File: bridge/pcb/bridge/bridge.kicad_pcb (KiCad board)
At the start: 2 copper layers, 108 x 80 mm, 26 parts, among them J1 Screw_Terminal_01x06, J2 Screw_Terminal_01x06, J3 Screw_Terminal_01x06, J4 Conn_01x23, J5 Conn_01x04, J6 Conn_01x02, J7 Conn_01x03, J8 Conn_01x02, J9 MCU_Test_Point, SW1 SW_SPST, U1 L293, U2 J104D2C12VDC.20S, U3 AD557JN, U4 ATmega328P-P

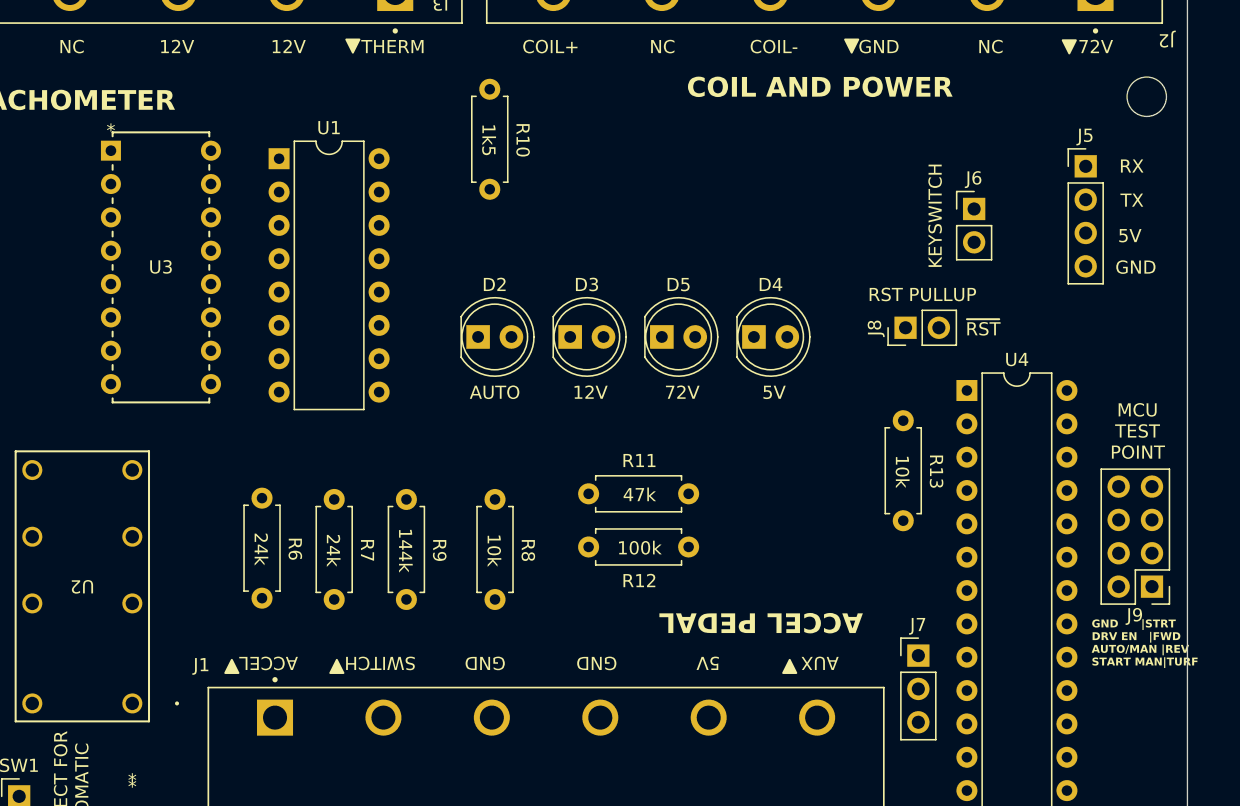
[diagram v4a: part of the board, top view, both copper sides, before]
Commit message: Assigned footprints and layed out board
Removed 5V and 12V enable headers as they added unneeded complexity
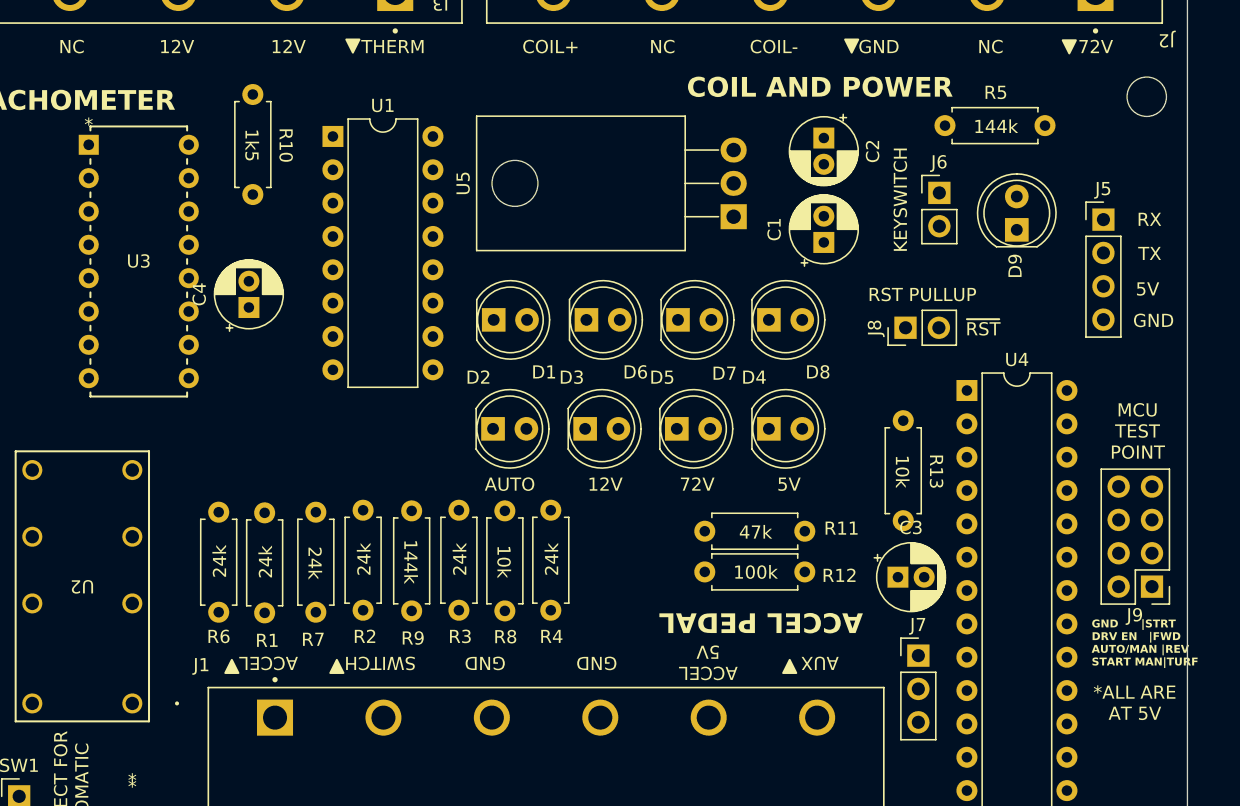
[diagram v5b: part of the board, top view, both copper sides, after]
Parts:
- added C1: 1u, Capacitor_THT:CP_Radial_D5.0mm_P2.00mm, F.Cu at (143.3, 72.8)
- added C2: 1u, Capacitor_THT:CP_Radial_D5.0mm_P2.00mm, F.Cu at (143.3, 64.8)
- added C3: 1u, Capacitor_THT:CP_Radial_D5.0mm_P2.00mm, F.Cu at (148.9, 98.3)
- added C4: 1u, Capacitor_THT:CP_Radial_D5.0mm_P2.00mm, F.Cu at (99.5, 77.8)
- added D1: GREEN, LED_THT:LED_D5.0mm, F.Cu at (118.2, 78.7)
- added D6: GREEN, LED_THT:LED_D5.0mm, F.Cu at (125.2, 78.7)
- added D7: GREEN, LED_THT:LED_D5.0mm, F.Cu at (132.2, 78.7)
- added D8: GREEN, LED_THT:LED_D5.0mm, F.Cu at (139.1, 78.7)
- added D9: GREEN, LED_THT:LED_D5.0mm, F.Cu at (158.0, 71.8)
- added R1: 24k, bridge:THT_RESISTOR_WITH_VALUE, F.Cu at (100.8, 97.2)
- added R2: 24k, bridge:THT_RESISTOR_WITH_VALUE, F.Cu at (108.3, 97.0)
- added R3: 24k, bridge:THT_RESISTOR_WITH_VALUE, F.Cu at (115.6, 97.0)
- added R4: 24k, bridge:THT_RESISTOR_WITH_VALUE, F.Cu at (122.6, 97.0)
- added R5: 144k, bridge:THT_RESISTOR_WITH_VALUE, F.Cu at (156.4, 64.0)
- added U5: L7805, Package_TO_SOT_THT:TO-220-3_Horizontal_TabDown, F.Cu at (136.4, 70.8)
- D2: value GREEN -> YELLOW
- D3, D4, D5: value GREEN -> RED
- moved R10 18.1 mm to (99.7, 65.4)
- moved R11 9.30 mm to (138.1, 94.9)
- moved R12 9.05 mm to (138.1, 98.0)
- moved D4 7.09 mm to (139.1, 87.0)
- moved D2 7.09 mm to (118.1, 87.0)
- moved D3 7.09 mm to (125.1, 87.0)
- moved D5 7.09 mm to (132.1, 87.0)
- moved U1 4.44 mm to (105.9, 64.7)
- moved J5 4.28 mm to (164.6, 71.1)
- moved R6 3.24 mm to (97.3, 97.1), turned to 90 degrees
- moved J6 2.92 mm to (152.1, 69.0)
- moved U3 1.75 mm to (87.3, 65.4)
- moved R7 1.70 mm to (104.5, 97.2)
- moved R8 1.15 mm to (118.9, 97.1)
- moved R9 0.96 mm to (111.8, 97.1)
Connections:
- J1 pad 5: +5V -> ACCEL_POT_5V
- J4 pad 9: +5V -> ACCEL_POT_5V
- U4 pad 25: unconnected-(U4-PC2-Pad25) -> ACCEL_POT_AUX
- U4 pad 26: unconnected-(U4-PC3-Pad26) -> ACCEL_AUX_MAN
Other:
- board text added: "*ALL ARE AT 5V"
- board text added: "ACCEL 5V"

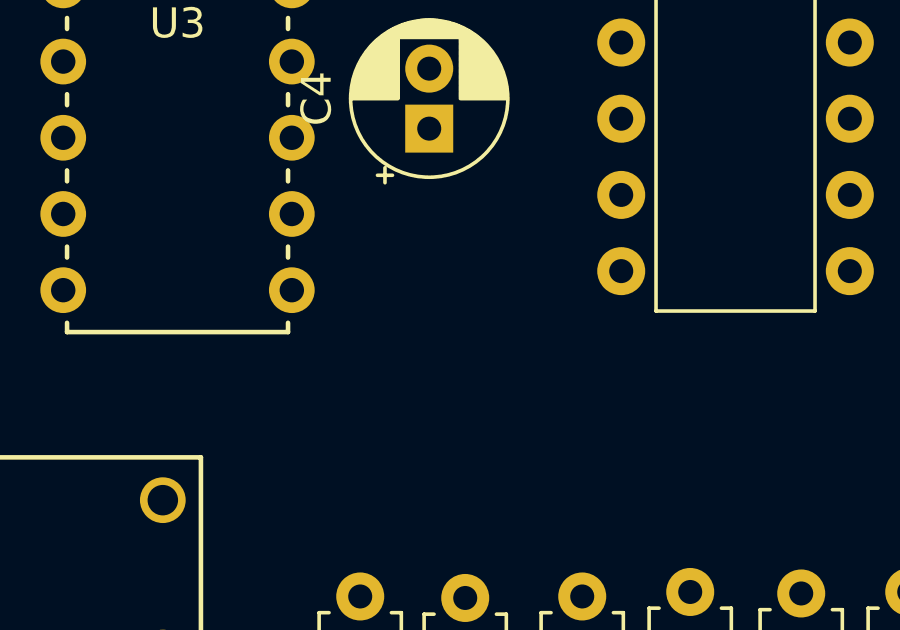
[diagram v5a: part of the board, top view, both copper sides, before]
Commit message: Added extra capacitor for L293
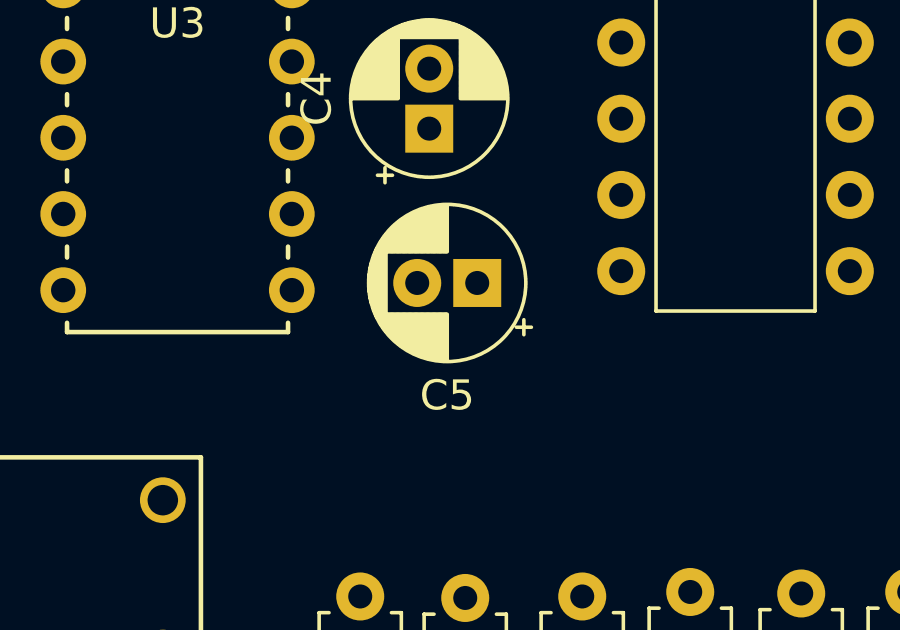
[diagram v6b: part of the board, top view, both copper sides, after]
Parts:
- added C5: 1u, Capacitor_THT:CP_Radial_D5.0mm_P2.00mm, F.Cu at (101.1, 82.9)

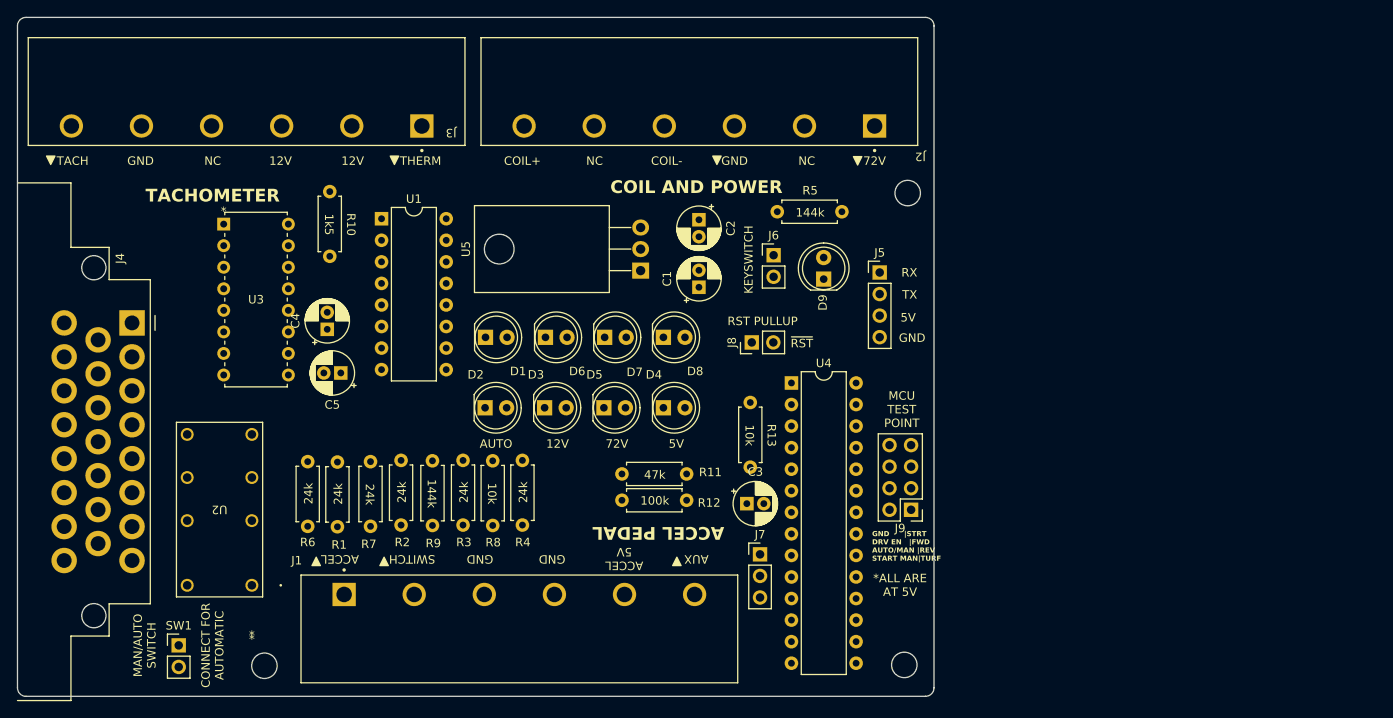
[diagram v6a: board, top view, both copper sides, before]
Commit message: Completed autorouter routing
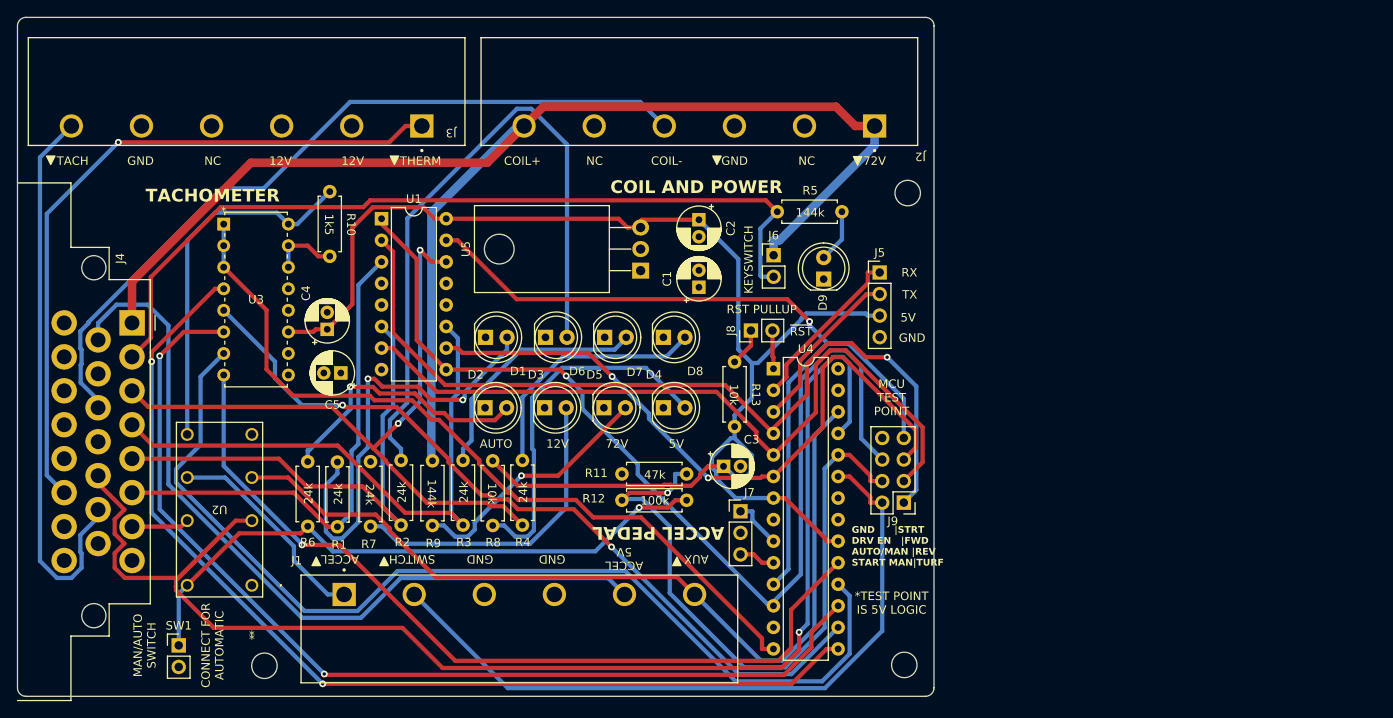
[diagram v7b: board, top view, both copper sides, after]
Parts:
- moved J7 5.57 mm to (148.2, 99.2)
- moved C3 5.19 mm to (146.2, 93.9)
- moved R13 5.13 mm to (147.4, 85.5)
- moved U4 2.70 mm to (152.1, 82.4)
- moved J8 1.40 mm to (149.4, 77.9)
- moved J9 1.20 mm to (167.4, 98.2)
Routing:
- net +5V: track 0.00 -> 171.2 mm
- net ACCEL_POT_AUX: track 0.00 -> 167.2 mm, vias 0 -> 1
- net +BATT: track 0.00 -> 166.9 mm
- net DRV_ENABLE: track 0.00 -> 122.1 mm, vias 0 -> 1
- net Net-(U3-BIT5): track 0.00 -> 121.5 mm, vias 0 -> 2
- net Net-(U3-BIT2): track 0.00 -> 120.6 mm
- net Net-(U3-BIT3): track 0.00 -> 119.2 mm, vias 0 -> 2
- net ACCEL_AUX_MAN: track 0.00 -> 103.6 mm
- net MCU_TURF: track 0.00 -> 101.2 mm, vias 0 -> 1
- net Net-(U3-(MSB)BIT1): track 0.00 -> 100.1 mm, vias 0 -> 1
- net KEYSWITCH: track 0.00 -> 98.4 mm
- net MCU_START: track 0.00 -> 97.6 mm, vias 0 -> 1
- net ACCEL_POT_5V: track 0.00 -> 93.9 mm
- net Net-(U3-BIT4): track 0.00 -> 93.8 mm, vias 0 -> 2
- net Net-(U3-(LSB)BIT8): track 0.00 -> 93.6 mm
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- added copper zone on In2.Cu, net +12V
- added copper zone on In1.Cu, net GND
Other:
- copper layers 2 -> 4
- board text added: "*TEST POINT IS 5V LOGIC"
- board text removed: "*ALL ARE AT 5V"

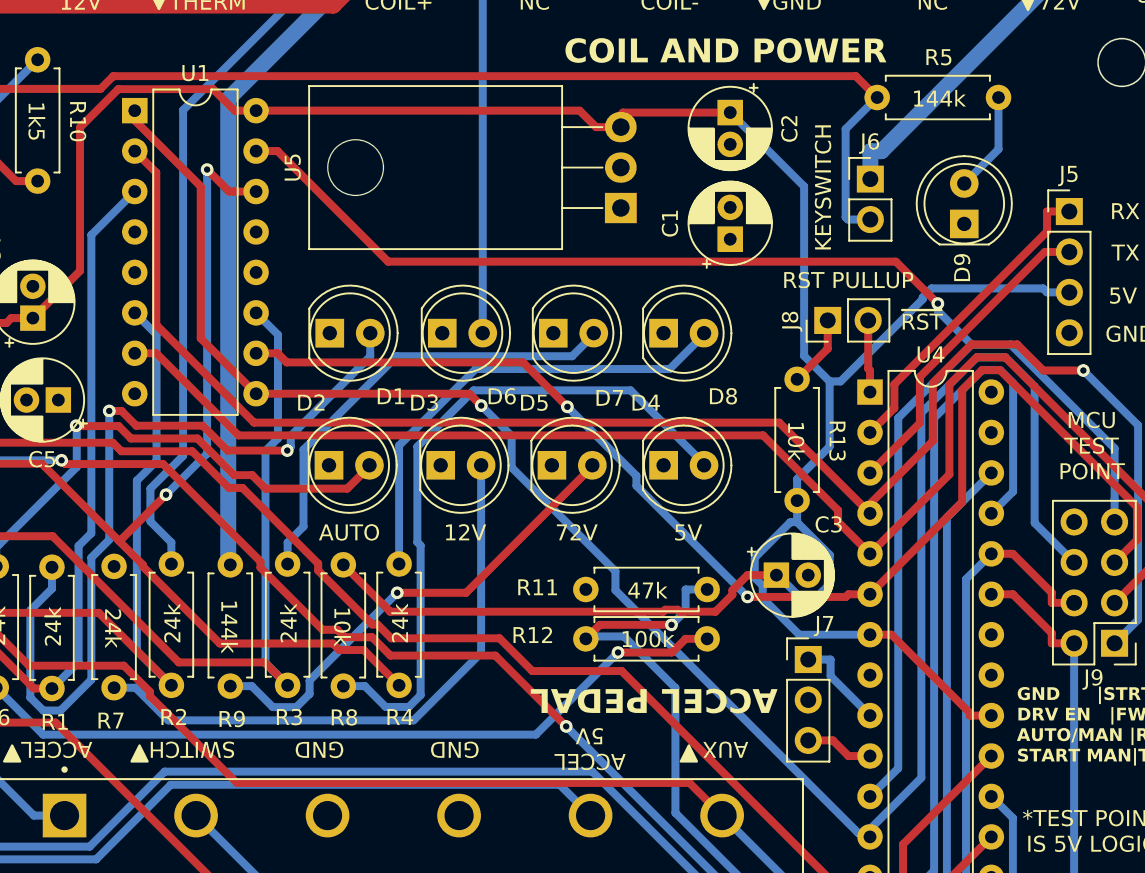
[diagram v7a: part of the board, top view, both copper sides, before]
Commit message: Added needed silkscreen labels for new design
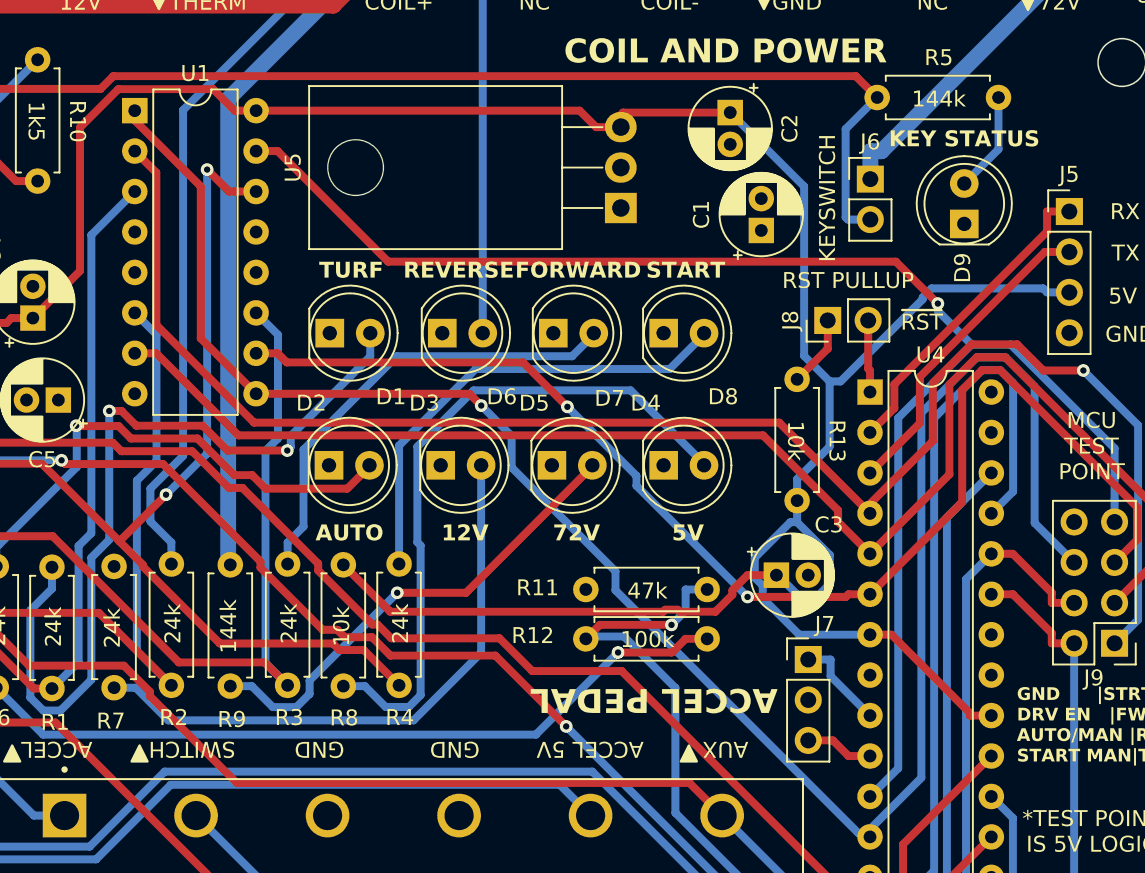
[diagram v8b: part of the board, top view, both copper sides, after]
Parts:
- moved C1 2.03 mm to (145.2, 72.2)
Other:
- board text added: "FORWARD"
- board text added: "KEY STATUS"
- board text added: "REVERSE"
- board text added: "START"
- board text added: "TURF"
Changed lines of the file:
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@@
         (effects (font (size 1 1) (thickness 0.1)))
     )
-    (fp_text value "24k" (at 0 0 -90 unlocked) (layer "F.SilkS")
+    (fp_text value "24k" (at 0 0 90 unlocked) (layer "F.SilkS")
         (effects (font (size 1 1) (thickness 0.15)))
     )
@@
   )
   (footprint "Capacitor_THT:CP_Radial_D5.0mm_P2.00mm" (layer "F.Cu")
-    (at 143.3 72.8 90)
+    (at 145.25 72.25 90)
     (descr "CP, Radial series, Radial, pin pitch=2.00mm, , diameter=5mm, Electrolytic Capacitor")
     (tags "CP Radial series Radial pin pitch 2.00mm  diameter 5mm Electrolytic Capacitor")
@@
         (effects (font (size 1 1) (thickness 0.1)))
     )
-    (fp_text value "10k" (at 0 0 -90 unlocked) (layer "F.SilkS")
+    (fp_text value "10k" (at 0 0 90 unlocked) (layer "F.SilkS")
         (effects (font (size 1 1) (thickness 0.15)))
     )
@@
         (effects (font (size 1 1) (thickness 0.1)))
     )
-    (fp_text value "144k" (at 0 0 -90 unlocked) (layer "F.SilkS")
+    (fp_text value "144k" (at 0 0 90 unlocked) (layer "F.SilkS")
         (effects (font (size 1 1) (thickness 0.15)))
     )
@@
     (effects (font (size 1 1) (thickness 0.15)) (justify left bottom))
   )
-  (gr_text "KEYSWITCH" (at 149.75 73.575 90) (layer "F.SilkS")
-    (effects (font (size 1 1) (thickness 0.15)) (justify left bottom))
+  (gr_text "KEYSWITCH" (at 150 74.25 90) (layer "F.SilkS")
+    (effects (font (size 1 1) (thickness 0.125)) (justify left bottom))
   )
   (gr_text "TACH" (at 69.5 58.5) (layer "F.SilkS")
@@
   )
   (gr_text "12V" (at 126.64 91.25) (layer "F.SilkS")
-    (effects (font (size 1 1) (thickness 0.15)))
+    (effects (font (size 1 1) (thickness 0.2) bold))
   )
   (gr_text "GND" (at 166.85 79.36) (layer "F.SilkS")
     (effects (font (size 1 1) (thickness 0.15)) (justify left bottom))
   )
+  (gr_text "KEY STATUS" (at 158 66.5) (layer "F.SilkS")
+    (effects (font (size 1 1) (thickness 0.2) bold))
+  )
   (gr_text "MAN/AUTO\nSWITCH" (at 78 115 90) (layer "F.SilkS")
     (effects (font (size 1 1) (thickness 0.15)))
   )
-  (gr_text "ACCEL\n5V" (at 134.5 103.4 180) (layer "F.SilkS")
+  (gr_text "ACCEL 5V" (at 134.5 104.25 180) (layer "F.SilkS")
     (effects (font (size 1 1) (thickness 0.15)) (justify bottom))
   )
@@
     (effects (font (size 1 1) (thickness 0.15)) (justify bottom))
   )
+  (gr_text "REVERSE" (at 126.25 74.75) (layer "F.SilkS")
+    (effects (font (size 1 1) (thickness 0.2) bold))
+  )
   (gr_text "COIL AND POWER" (at 143 61) (layer "F.SilkS")
     (effects (font (size 1.5 1.5) (thickness 0.3) bold))
   )
   (gr_text "72V" (at 133.64 91.25) (layer "F.SilkS")
-    (effects (font (size 1 1) (thickness 0.15)))
+    (effects (font (size 1 1) (thickness 0.2) bold))
   )
   (gr_text "5V" (at 140.64 91.25) (layer "F.SilkS")
-    (effects (font (size 1 1) (thickness 0.15)))
+    (effects (font (size 1 1) (thickness 0.2) bold))
   )
   (gr_text "72V" (at 164 58.5) (layer "F.SilkS")
@@
     (effects (font (size 1 1) (thickness 0.15)))
   )
+  (gr_text "TURF" (at 119.5 74.75) (layer "F.SilkS")
+    (effects (font (size 1 1) (thickness 0.2) bold))
+  )
   (gr_text "SWITCH" (at 109.5 104.25 180) (layer "F.SilkS")
     (effects (font (size 1 1) (thickness 0.15)) (justify bottom))
@@
   )
   (gr_text "AUTO" (at 119.39 91.25) (layer "F.SilkS")
-    (effects (font (size 1 1) (thickness 0.15)))
+    (effects (font (size 1 1) (thickness 0.2) bold))
   )
   (gr_text "GND" (at 117.5 104.25 180) (layer "F.SilkS")
     (effects (font (size 1 1) (thickness 0.15)) (justify bottom))
   )
+  (gr_text "FORWARD" (at 133.75 74.75) (layer "F.SilkS")
+    (effects (font (size 1 1) (thickness 0.2) bold))
+  )
+  (gr_text "START" (at 140.5 74.75) (layer "F.SilkS")
+    (effects (font (size 1 1) (thickness 0.2) bold))
+  )
   (gr_text "ACCEL PEDAL" (at 138.5 101.75 180) (layer "F.SilkS")
